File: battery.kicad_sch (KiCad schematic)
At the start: 19 parts, among them J1 Conn_01x04_Female, J2 Conn_02x05_Odd_Even, J3 Conn_02x03_Odd_Even, J4 Conn_01x06_Male, J5 Conn_01x02_Female, Q2 Q_NMOS_GSD, U1 AP3428

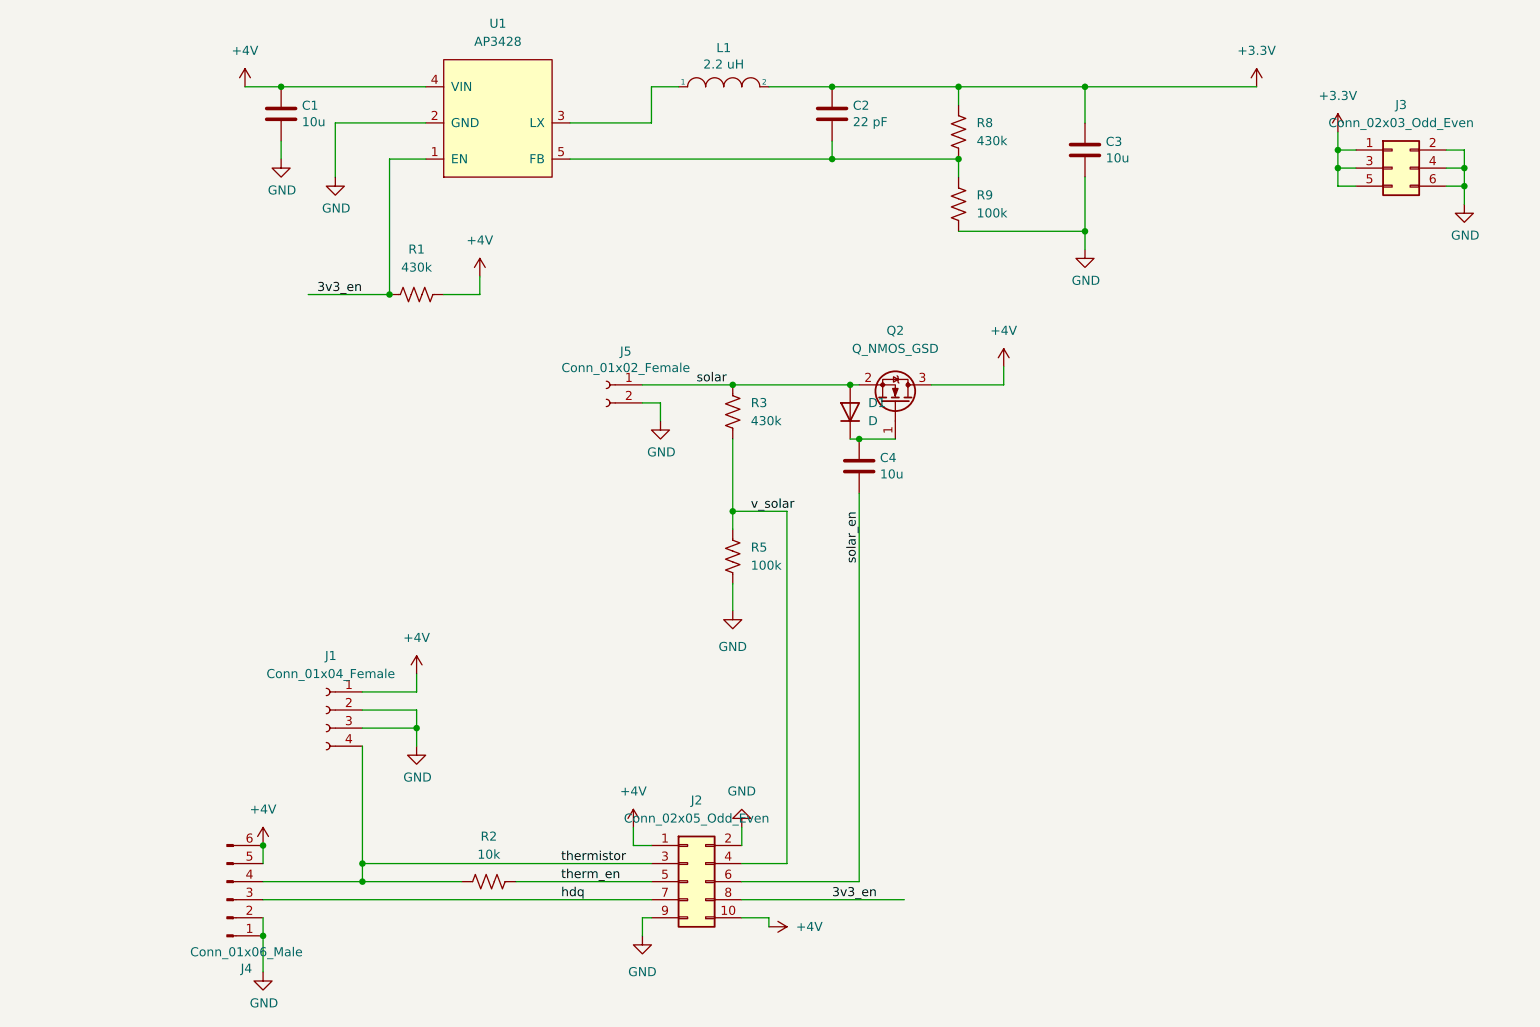
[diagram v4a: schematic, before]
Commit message: Simplified board, switched to JST PH connector
Also upgraded to KiCad 7.0
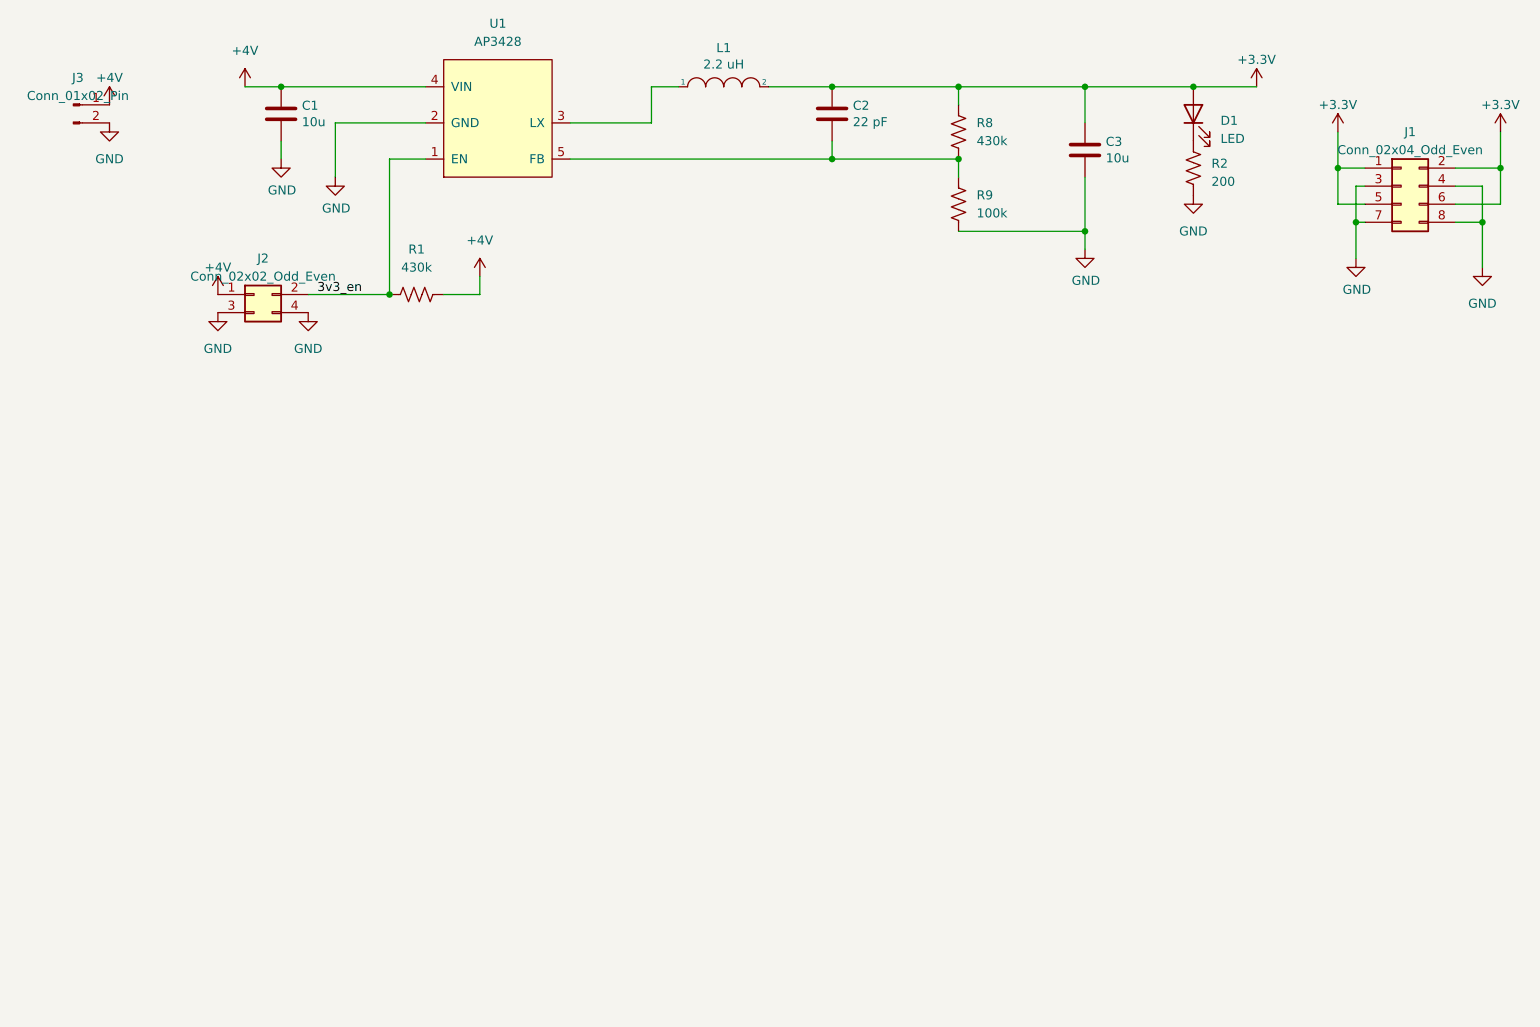
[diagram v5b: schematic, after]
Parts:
- removed C4: 10u, Capacitor_SMD:C_0805_2012Metric, symbol Device:C
- removed D1: D, Diode_SMD:D_SOD-323, symbol Device:D
- removed J1: Conn_01x04_Female, Connector_PinHeader_2.54mm:PinHeader_1x04_P2.54mm_Vertical, symbol Connector:Conn_01x04_Female
- removed J2: Conn_02x05_Odd_Even, Connector_PinHeader_2.54mm:PinHeader_2x05_P2.54mm_Vertical_SMD, symbol Connector_Generic:Conn_02x05_Odd_Even
- removed J3: Conn_02x03_Odd_Even, Connector_PinHeader_2.54mm:PinHeader_2x03_P2.54mm_Vertical, symbol Connector_Generic:Conn_02x03_Odd_Even
- removed J4: Conn_01x06_Male, battery:battery_connector, symbol Connector:Conn_01x06_Male
- removed J5: Conn_01x02_Female, Connector_PinSocket_2.54mm:PinSocket_1x02_P2.54mm_Vertical, symbol Connector:Conn_01x02_Female
- removed Q2: Q_NMOS_GSD, Package_TO_SOT_SMD:SOT-23, symbol Device:Q_NMOS_GSD
- removed R3: 430k, Resistor_SMD:R_0603_1608Metric, symbol Device:R_US
- removed R5: 100k, Resistor_SMD:R_0603_1608Metric, symbol Device:R_US
- added D1: LED, LED_SMD:LED_0603_1608Metric, symbol Device:LED
- added J1: Conn_02x04_Odd_Even, Connector_PinHeader_2.54mm:PinHeader_2x04_P2.54mm_Vertical, symbol Connector_Generic:Conn_02x04_Odd_Even
- added J2: Conn_02x02_Odd_Even, Connector_PinHeader_2.54mm:PinHeader_2x02_P2.54mm_Vertical, symbol Connector_Generic:Conn_02x02_Odd_Even
- added J3: Conn_01x02_Pin, Connector_JST:JST_PH_S2B-PH-K_1x02_P2.00mm_Horizontal, symbol Connector:Conn_01x02_Pin
- R2: value 10k -> 200
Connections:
- net thermistor is gone; now on net GND: R2.2
- net +4V: now also J2.1 (Pin_1), J3.1 (Pin_1)
- net 3v3_en: now also J2.2 (Pin_2)
- net GND: now also J1.3 (Pin_3), J1.4 (Pin_4), J1.7 (Pin_7), J1.8 (Pin_8), J2.3 (Pin_3), J2.4 (Pin_4), J3.2 (Pin_2)
- net +3V3 renamed +3.3V
- net +3.3V: now also D1.2 (A), J1.1 (Pin_1), J1.2 (Pin_2), J1.5 (Pin_5), J1.6 (Pin_6)
- net therm_en: no longer names the net of R2.1
- net therm_en: now also D1.1 (K)
